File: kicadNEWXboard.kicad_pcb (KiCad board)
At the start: 2 copper layers, 217.5 x 131.8 mm, 112 parts, among them SW1 SW_Push, U1 ATmega32U4-AU, Y1 16MHz

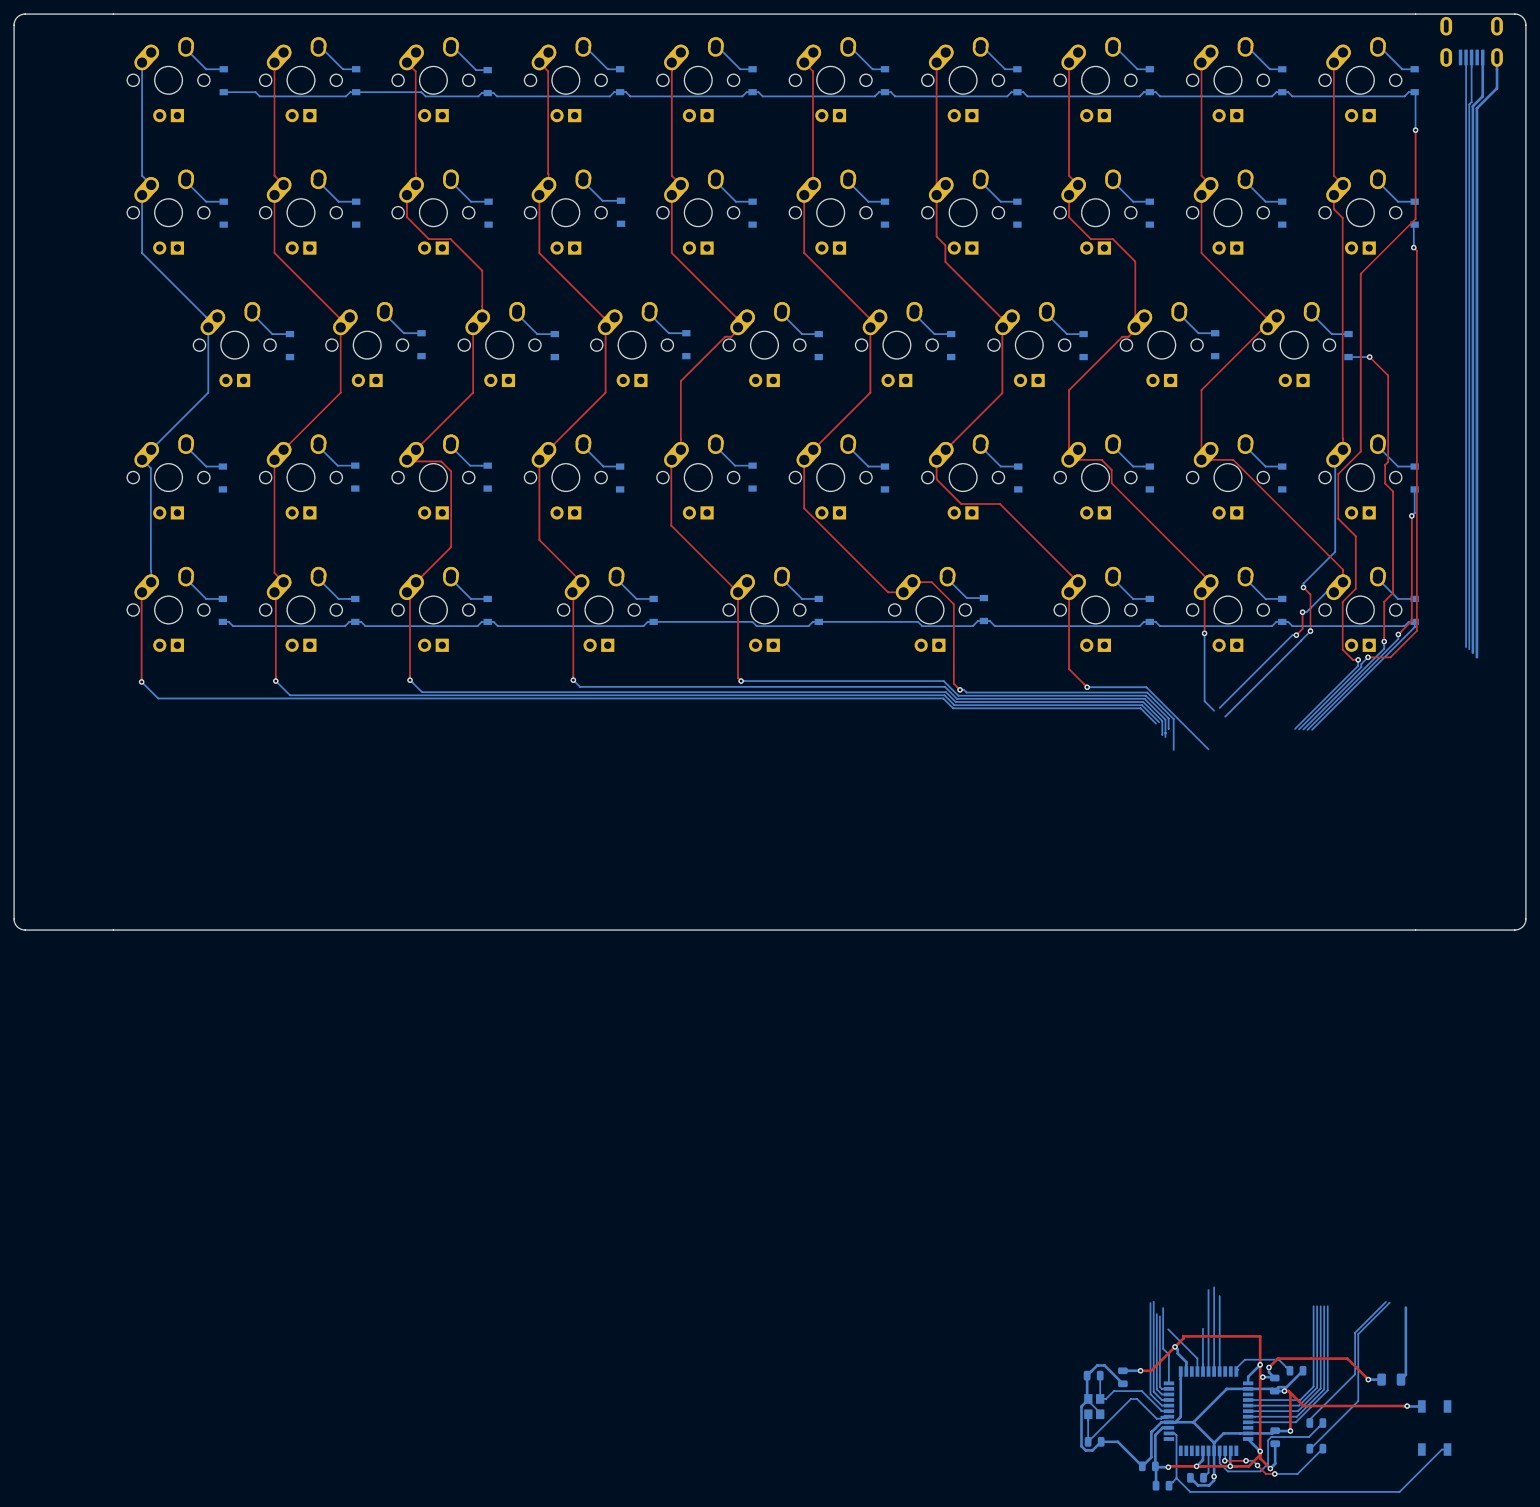
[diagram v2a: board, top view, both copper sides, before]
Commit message: added hotswap submod
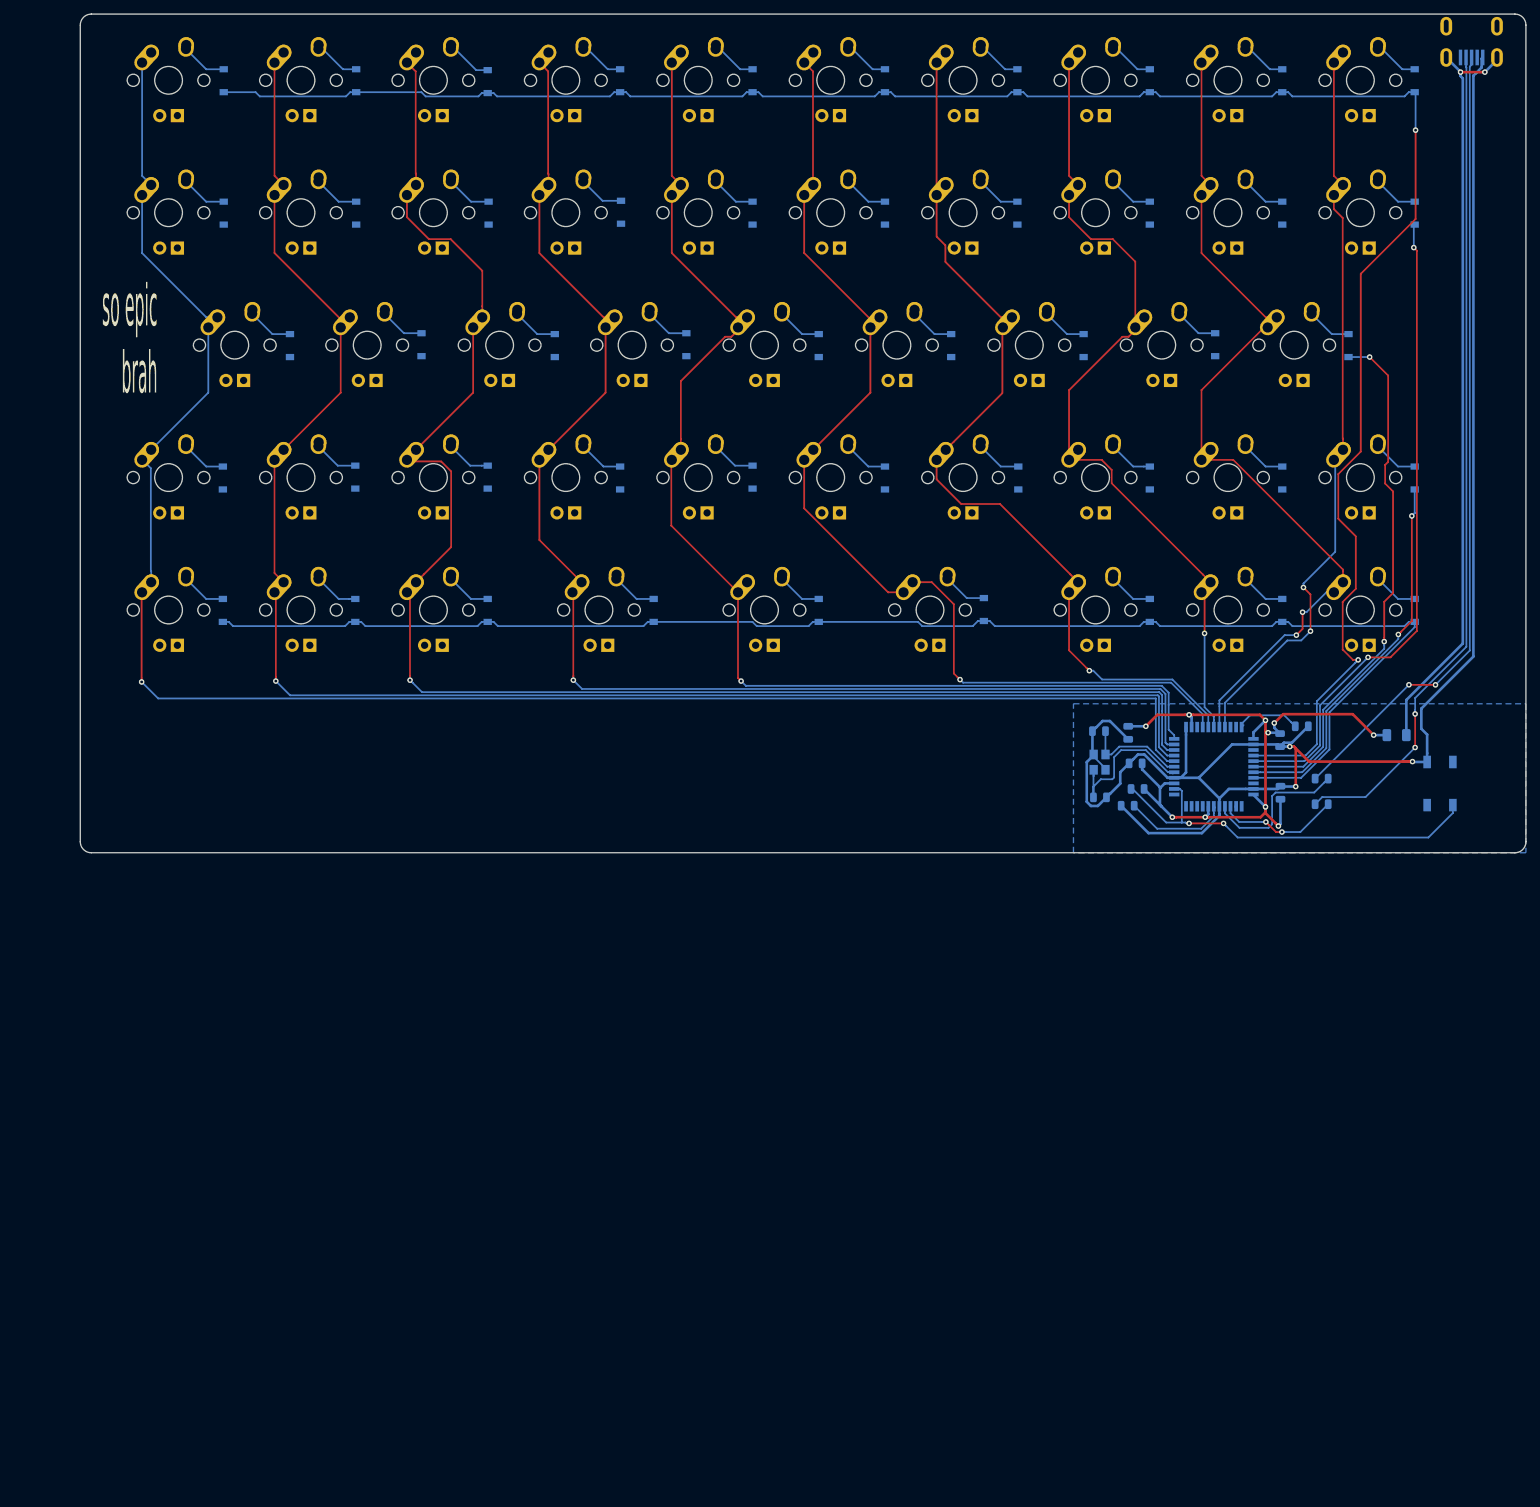
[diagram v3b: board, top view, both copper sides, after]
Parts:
- moved C2 101.1 mm to (183.6, 134.0)
- moved R3 100.3 mm to (183.8, 137.7), turned to 0 degrees
- moved C6 97.2 mm to (182.4, 140.1)
- moved C3 92.7 mm to (178.3, 129.3)
- moved C5 92.7 mm to (204.3, 130.6)
- moved C7 92.7 mm to (204.4, 138.2)
- moved F1 92.7 mm to (221.1, 129.9)
- moved R1 92.7 mm to (210.3, 139.9)
- moved R2 92.7 mm to (210.3, 136.2)
- moved SW1 92.7 mm to (227.4, 136.9)
- moved Y1 92.7 mm to (178.4, 133.8)
- moved C1 92.7 mm to (182.5, 129.6)
- moved C4 92.7 mm to (178.4, 138.9)
- moved R4 92.7 mm to (207.5, 128.7)
- moved U1 92.7 mm to (194.8, 134.5)
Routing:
- net GND: track 210.4 -> 238.4 mm, vias 4 -> 3
- net ROW3: track 65.5 -> 54.4 mm
- net ROW1: track 104.4 -> 93.3 mm
- net Net-(C6-Pad1): track 4.19 -> 15.3 mm
- net ROW0: track 300.7 -> 289.7 mm
- net ROW2: track 87.3 -> 76.3 mm
- net ROW4: track 222.7 -> 211.6 mm
- net VCC: track 98.1 -> 108.8 mm, vias 0 -> 2
- net D-: track 110.6 -> 120.2 mm, vias 0 -> 2
- net COL7: track 125.4 -> 116.0 mm
- net COL8: track 130.0 -> 121.3 mm
- net D+: track 107.2 -> 115.8 mm, vias 0 -> 2
- net +5V: track 110.3 -> 101.9 mm, vias 11 -> 10
- net COL9: track 110.6 -> 102.4 mm
- net COL6: track 134.4 -> 126.3 mm
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- added copper zone on B.Cu, net GND
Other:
- board size 217.5 x 131.8 mm -> 208 x 120.7 mm
- board text added: "newk board 03 the awesomester one yet !!!!1!"
- board text added: "so epic brah"

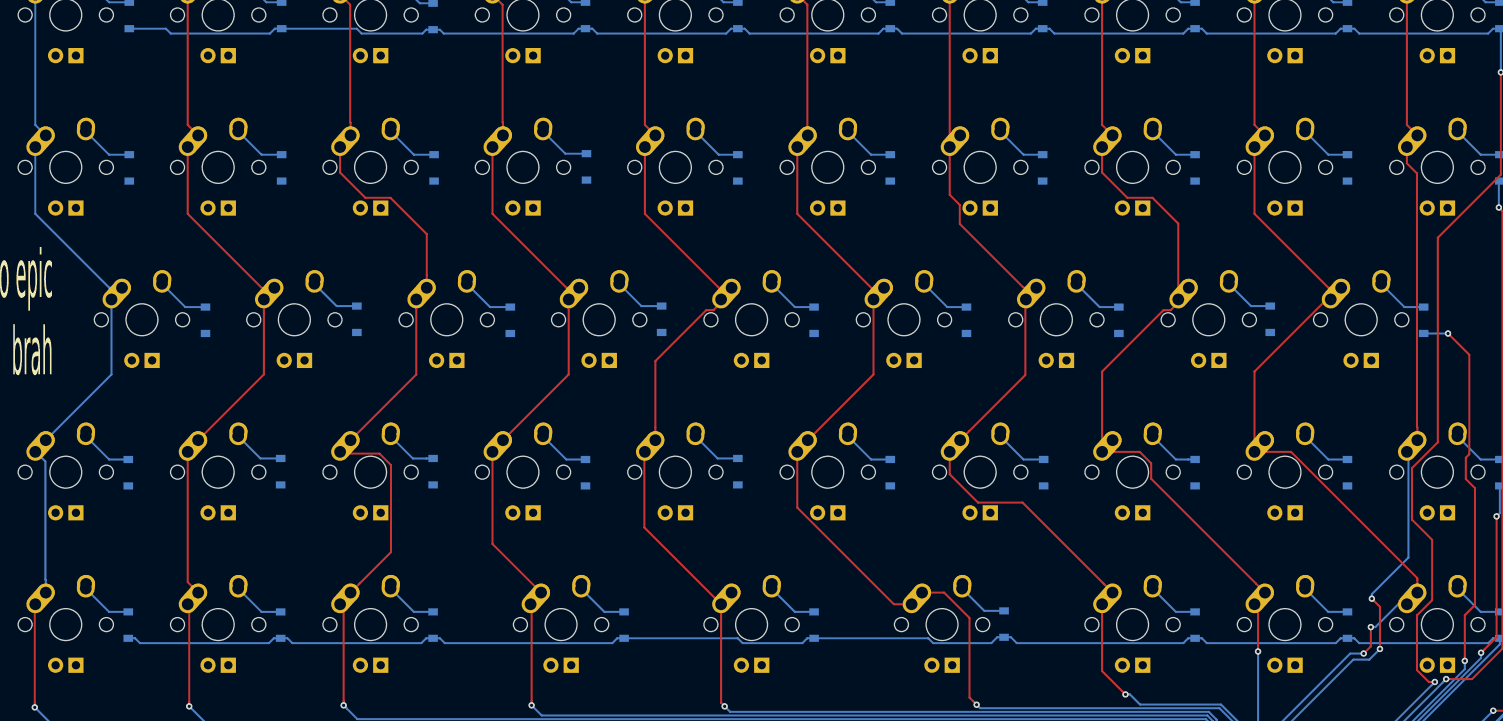
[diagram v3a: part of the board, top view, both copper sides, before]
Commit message: push before updating kicad vers
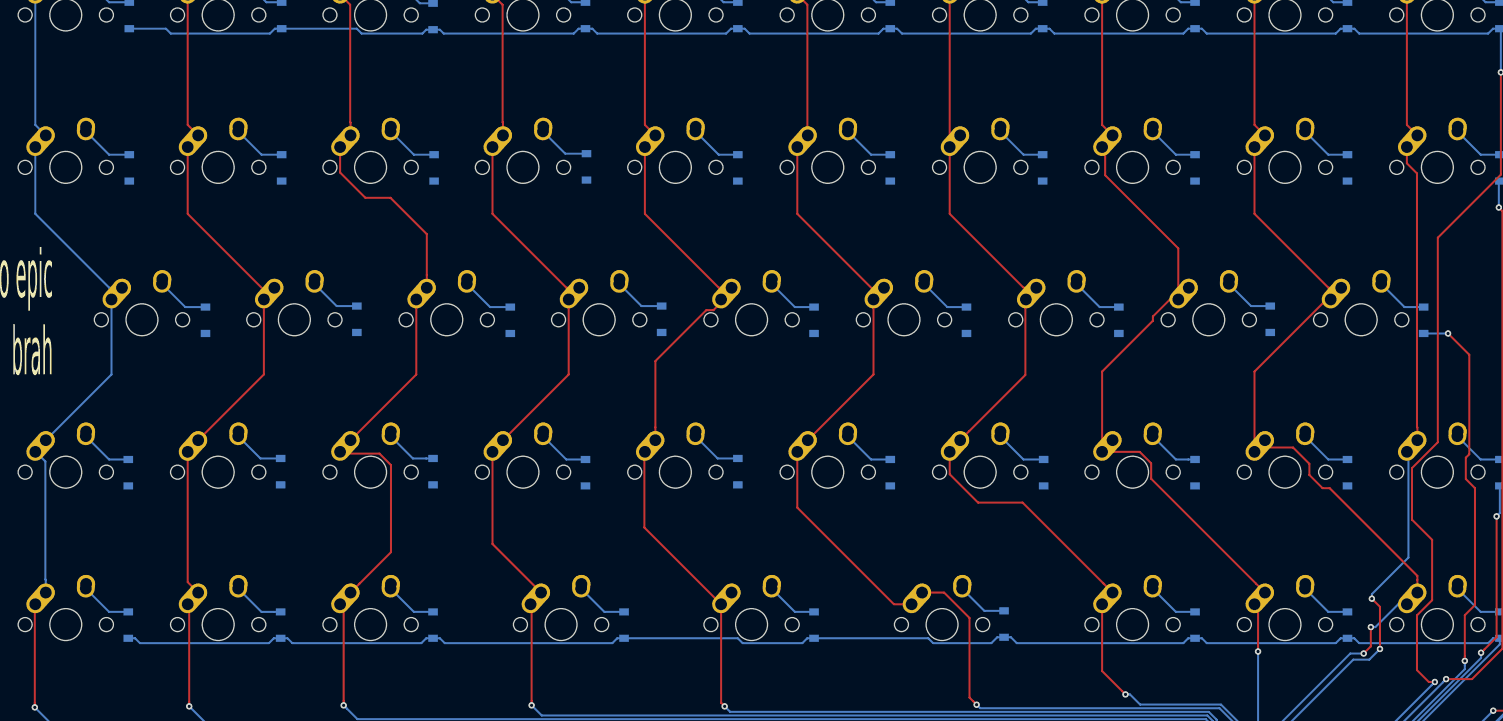
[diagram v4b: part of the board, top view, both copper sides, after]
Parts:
- MX1, MX10, MX11, MX12, MX13, MX14, MX15, MX16, MX17, MX18, MX19, MX2, MX20, MX21, MX22, MX23, MX24, MX25, MX26, MX27, MX28, MX29, MX3, MX30, MX31, MX32, MX33, MX34, MX35, MX36, MX37, MX38, MX39, MX4, MX40, MX41, MX42, MX43, MX44, MX45, MX46, MX47, MX48, MX5, MX6, MX7, MX8, MX9: footprint MX_Alps_Hybrid:MX-1U -> MX_Alps_Hybrid:MX-1U-NoLED
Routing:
- net COL7: track 116.0 -> 114.3 mm
- net COL8: track 121.3 -> 122.7 mm

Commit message: lots of stuff
updated to new KiCad version
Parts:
- MX1, MX10, MX11, MX12, MX13, MX14, MX15, MX16, MX17, MX18, MX19, MX2, MX21, MX22, MX23, MX24, MX25, MX26, MX27, MX28, MX29, MX3, MX31, MX32, MX33, MX34, MX35, MX36, MX37, MX38, MX39, MX4, MX40, MX41, MX42, MX43, MX44, MX45, MX46, MX47, MX48, MX5, MX6, MX7, MX8, MX9: footprint MX_Alps_Hybrid:MX-1U-NoLED -> MX_Hotswap:MX-Hotswap-1U
- MX20, MX30: footprint MX_Alps_Hybrid:MX-1U-NoLED -> MX_Hotswap:MX-Hotswap-1.5U
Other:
- net class Default removed
- net class Power removed
- rule pad_to_mask_clearance: 0.051 -> 0
- board text added: "newk board 04 - the most awesomester one yet so far1 !!!!1!"
- board text added: "so epic brah fr"
- board text removed: "newk board 03 the awesomester one yet !!!!1!"
- board text removed: "so epic brah"
